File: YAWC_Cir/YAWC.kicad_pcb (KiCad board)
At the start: 2 copper layers, 84 x 35 mm, 32 parts, among them P1 CONN_01X03, P2 TP1a, P3 CONN_5, P4 CONN_5, P5 CONN_6, P6 TP1b, P7 J_AllOff, P8 J_Pot, U1 TPS769XX, U2 SAMD20J18A-M

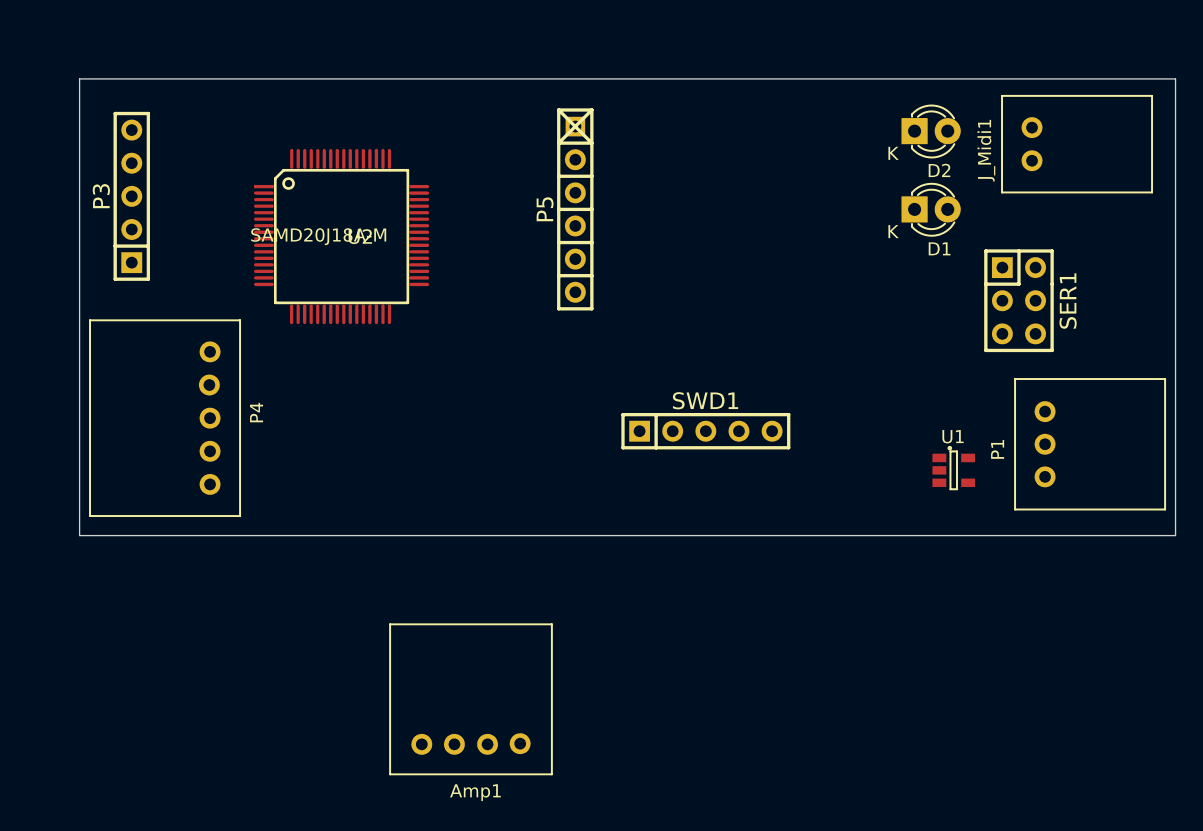
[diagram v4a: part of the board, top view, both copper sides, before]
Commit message: More work on main PCB and positioned connectors to match Keys
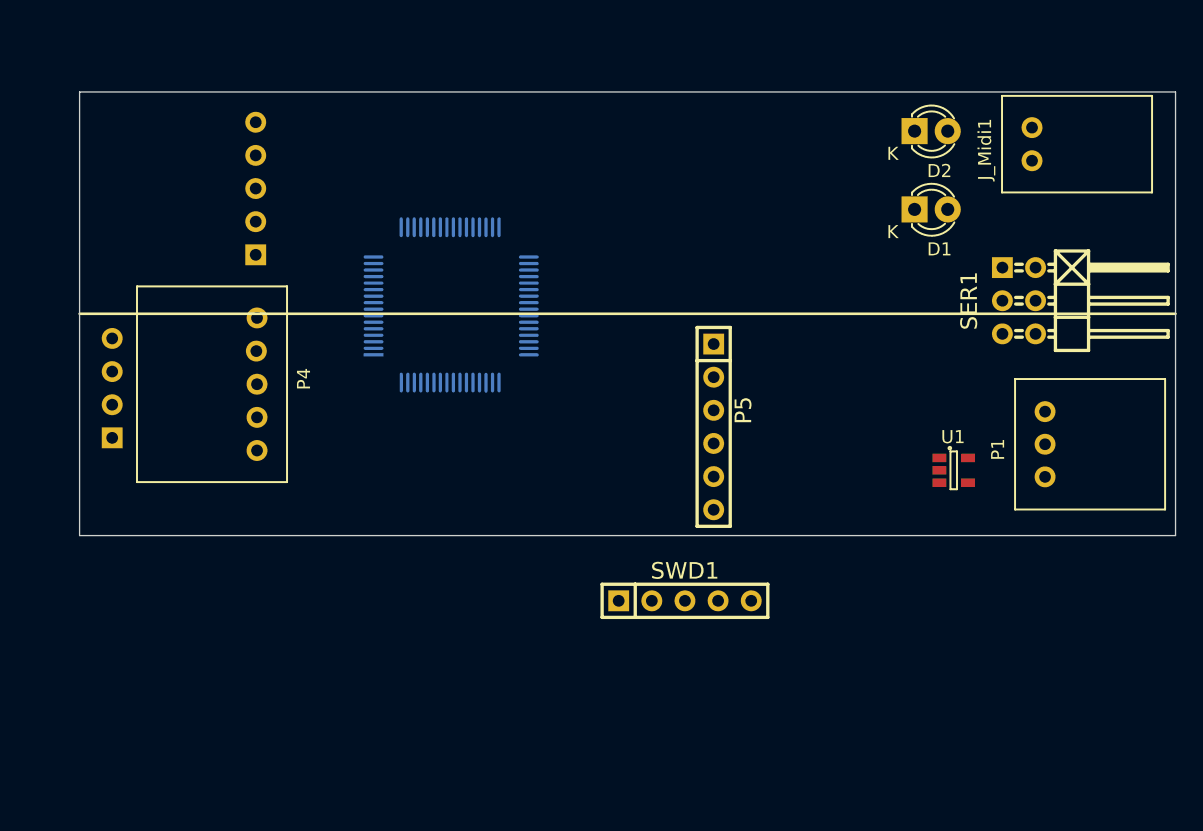
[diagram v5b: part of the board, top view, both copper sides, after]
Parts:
- Amp1: footprint JST:S4B-XH -> PIN_Hdr:Pin_Header_Straight_1x04; moved to B.Cu
- P3, U2: moved to B.Cu
- P5: footprint PIN_Hdr:Pin_Header_1x06 -> PIN_Hdr:Pin_Header_Straight_1x06
- SER1: footprint PIN_Hdr:Pin_Header_Straight_2x03 -> PIN_Hdr:Pin_Header_Angled_2x03
- moved Amp1 38.7 mm to (77.5, 120.7), turned to 90 degrees
- moved P5 18.7 mm to (123.6, 122.4)
- moved SWD1 13.1 mm to (121.4, 137.0)
- moved U2 9.99 mm to (103.4, 114.4), turned to 90 degrees
- moved P3 9.52 mm to (88.5, 105.4)
- moved P4 4.44 mm to (88.6, 120.4)
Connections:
- P3 pad 1: /Micro/Y14 -> /Micro/Y15
- P3 pad 2: /Micro/Y13 -> /Micro/Y2
- P3 pad 3: /Micro/Y12 -> /Micro/Y3
- P3 pad 4: /Micro/Y11 -> /Micro/Y4
- P3 pad 5: /Micro/Y10 -> /Micro/Y5
- P4 pad 1: /Micro/Y15 -> /Micro/Y10
- P4 pad 2: /Micro/Y2 -> /Micro/Y11
- P4 pad 3: /Micro/Y3 -> /Micro/Y12
- P4 pad 4: /Micro/Y4 -> /Micro/Y13
- P4 pad 5: /Micro/Y5 -> /Micro/Y14
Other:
- board size 84 x 35 mm -> 84 x 34 mm

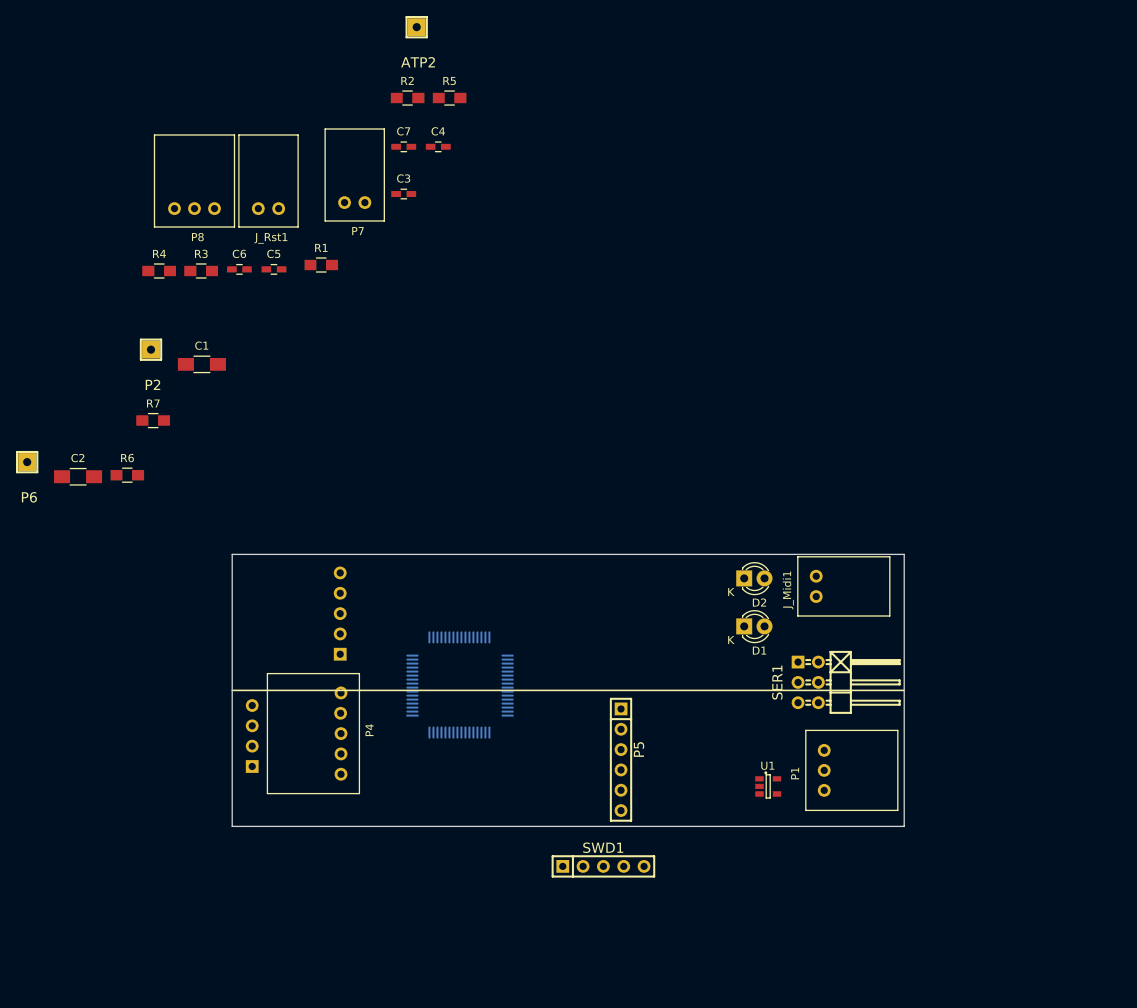
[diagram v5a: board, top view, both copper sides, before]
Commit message: move parts nearer final positions
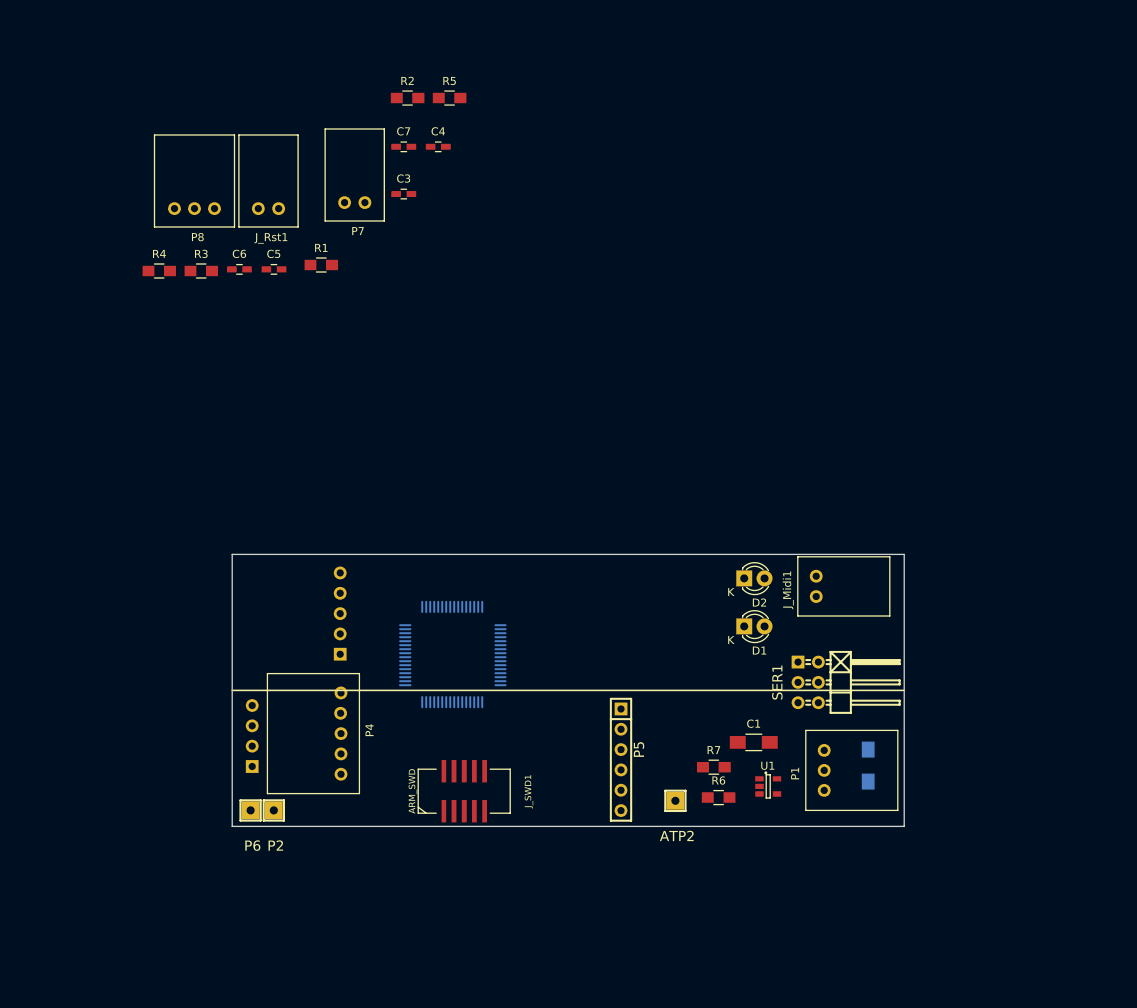
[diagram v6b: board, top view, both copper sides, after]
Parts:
- removed SWD1: CONN_5, PIN_Hdr:Pin_Header_Straight_1x05
- added J_SWD1: ARM_SWD, My_Pin_Headers:2x5_50mil_SMD, F.Cu at (104.0, 127.6)
- C2: moved to B.Cu
- moved C2 105.2 mm to (154.5, 124.4), turned to 90 degrees
- moved ATP2 102.0 mm to (130.4, 128.8)
- moved R6 84.2 mm to (135.8, 128.4)
- moved C1 83.6 mm to (140.2, 121.5)
- moved R7 82.4 mm to (135.2, 124.6)
- moved P2 59.6 mm to (80.2, 130.0)
- moved P6 51.7 mm to (77.3, 130.0)
- moved U2 3.91 mm to (102.5, 110.6)
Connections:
- C1 pad 1: GND -> /VBatt
- P1 pad 3: GND -> /VBatt
- R6 pad 1: GND -> /VBatt
- U1 pad 1: GND -> /VBatt
- U1 pad 4: (no net) -> Net-(U1-Pad4)
- U2 pad 1: (no net) -> Net-(U2-Pad1)
- U2 pad 2: (no net) -> Net-(U2-Pad2)
- U2 pad 23: (no net) -> Net-(U2-Pad23)
- U2 pad 25: (no net) -> Net-(U2-Pad25)
- U2 pad 26: (no net) -> Net-(U2-Pad26)
- U2 pad 27: (no net) -> Net-(U2-Pad27)
- U2 pad 28: (no net) -> Net-(U2-Pad28)
- U2 pad 30: (no net) -> Net-(U2-Pad30)
- U2 pad 31: (no net) -> Net-(U2-Pad31)
- U2 pad 32: (no net) -> Net-(U2-Pad32)
- U2 pad 39: (no net) -> Net-(U2-Pad39)
- U2 pad 40: (no net) -> Net-(U2-Pad40)
- U2 pad 41: (no net) -> Net-(U2-Pad41)
- U2 pad 42: (no net) -> Net-(U2-Pad42)
- U2 pad 43: (no net) -> Net-(U2-Pad43)
- U2 pad 44: (no net) -> Net-(U2-Pad44)
- U2 pad 45: (no net) -> Net-(U2-Pad45)
- U2 pad 46: (no net) -> Net-(U2-Pad46)
- U2 pad 49: (no net) -> Net-(U2-Pad49)
- U2 pad 50: (no net) -> Net-(U2-Pad50)
- U2 pad 51: (no net) -> Net-(U2-Pad51)
- U2 pad 53: (no net) -> Net-(U2-Pad53)

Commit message: Routed but no copper pour
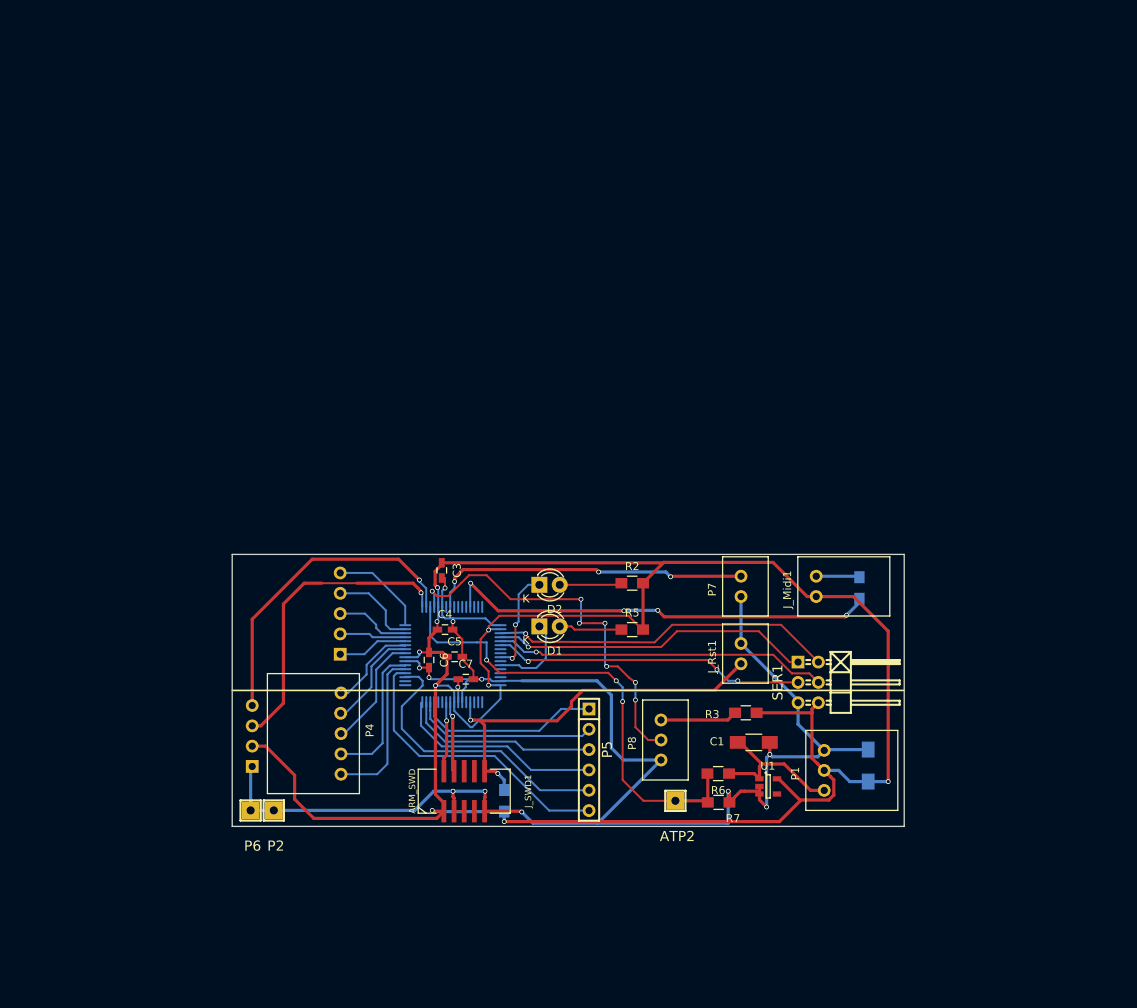
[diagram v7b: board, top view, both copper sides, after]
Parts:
- J_Rst1, P7: footprint JST:S2B-XH -> JST:B2B-XH
- P8: footprint JST:S3B-XH -> JST:B3B-XH
- R1, R4: moved to B.Cu
- moved R4 96.1 mm to (153.4, 102.2), turned to 270 degrees
- moved P8 88.4 mm to (128.6, 121.2), turned to 270 degrees
- moved R3 87.7 mm to (139.2, 117.8), turned to 180 degrees
- moved J_Rst1 81.1 mm to (138.6, 110.4), turned to 270 degrees
- moved R1 70.8 mm to (109.0, 128.8), turned to 90 degrees
- moved R5 70.3 mm to (125.0, 107.4)
- moved P7 68.1 mm to (138.6, 102.0), turned to 270 degrees
- moved C7 67.0 mm to (104.2, 113.6)
- moved R2 66.8 mm to (125.0, 101.6)
- moved C4 60.4 mm to (101.6, 107.4)
- moved C6 54.3 mm to (99.6, 111.2), turned to 270 degrees
- moved C5 53.4 mm to (102.8, 110.8)
- moved C3 47.3 mm to (101.2, 100.0), turned to 270 degrees
- moved D2 25.6 mm to (113.4, 101.8)
- moved D1 25.6 mm to (113.4, 107.0)
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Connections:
- J_SWD1 pad 6: Net-(J_SWD1-Pad6) -> (no net)
- J_SWD1 pad 7: Net-(J_SWD1-Pad7) -> (no net)
- J_SWD1 pad 8: Net-(J_SWD1-Pad8) -> (no net)
- P8 pad 2: Net-(P8-Pad2) -> /Micro/Pot
- R5 pad 1: Net-(D1-Pad1) -> Net-(D1-Pad2)
- SER1 pad 1: /Micro/S1P3 -> /Micro/S1P1
- SER1 pad 2: /Micro/S1P2 -> /Micro/S1P0
- SER1 pad 3: /Micro/S1P1 -> /Micro/S1P3
- SER1 pad 4: /Micro/S1P0 -> /Micro/S1P2
- U1 pad 4: Net-(U1-Pad4) -> (no net)
- U2 pad 1: Net-(U2-Pad1) -> (no net)
- U2 pad 17: Net-(P8-Pad2) -> Bth
- U2 pad 18: BatSample -> Vib
- U2 pad 19: Vib -> BatSample
- U2 pad 2: Net-(U2-Pad2) -> (no net)
- U2 pad 20: Bth -> /Micro/Pot
- U2 pad 23: Net-(U2-Pad23) -> (no net)
- U2 pad 25: Net-(U2-Pad25) -> (no net)
- U2 pad 26: Net-(U2-Pad26) -> (no net)
- U2 pad 27: Net-(U2-Pad27) -> (no net)
- U2 pad 28: Net-(U2-Pad28) -> (no net)
- U2 pad 30: Net-(U2-Pad30) -> (no net)
- U2 pad 31: Net-(U2-Pad31) -> (no net)
- U2 pad 32: Net-(U2-Pad32) -> (no net)
- U2 pad 39: Net-(U2-Pad39) -> (no net)
- U2 pad 40: Net-(U2-Pad40) -> (no net)
- U2 pad 41: Net-(U2-Pad41) -> Net-(D2-Pad1)
- U2 pad 42: Net-(U2-Pad42) -> (no net)
- U2 pad 43: Net-(U2-Pad43) -> Net-(D1-Pad1)
- U2 pad 44: Net-(U2-Pad44) -> (no net)
- U2 pad 45: Net-(U2-Pad45) -> (no net)
- U2 pad 46: Net-(U2-Pad46) -> (no net)
- U2 pad 49: Net-(U2-Pad49) -> (no net)
- U2 pad 50: Net-(U2-Pad50) -> (no net)
- U2 pad 51: Net-(U2-Pad51) -> (no net)
- U2 pad 53: Net-(U2-Pad53) -> (no net)
- U2 pad 59: Net-(D1-Pad2) -> (no net)
- U2 pad 60: Net-(D2-Pad1) -> (no net)
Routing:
- net VCC: track 0.00 -> 289.8 mm, vias 0 -> 9
- net GND: track 0.00 -> 210.2 mm, vias 0 -> 11
- net BatSample: track 0.00 -> 58.6 mm, vias 0 -> 3
- net /Micro/Tx: track 0.00 -> 54.6 mm, vias 0 -> 4
- net /Micro/Reset: track 0.00 -> 50.2 mm, vias 0 -> 2
- net /Micro/Pot: track 0.00 -> 49.0 mm, vias 0 -> 7
- net /Micro/S1P0: track 0.00 -> 43.4 mm, vias 0 -> 1
- net /Micro/S1P2: track 0.00 -> 41.9 mm, vias 0 -> 1
- net Net-(P7-Pad1): track 0.00 -> 40.5 mm, vias 0 -> 3
- net /Micro/S1P1: track 0.00 -> 40.1 mm, vias 0 -> 1
- net Vib: track 0.00 -> 39.6 mm, vias 0 -> 1
- net /Micro/S1P3: track 0.00 -> 39.4 mm, vias 0 -> 3
- net Bth: track 0.00 -> 38.6 mm, vias 0 -> 1
- net /Micro/Y1: track 0.00 -> 36.9 mm
- net /Micro/Y0: track 0.00 -> 36.1 mm
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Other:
- net class Default: trace_width 0.25 -> 0.4
- net class Sense added: clearance 0.2, trace_width 0.25, via_dia 0.6, via_drill 0.4

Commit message: As subbmitted to OSH Park
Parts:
- All Off: renamed from P7
- renumbered ATP2 to ATP, J_Midi1 to Midi, P8 to Pot, P1 to Pwr, J_Rst1 to Rst
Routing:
- net GND: track 210.2 -> 258.7 mm
- added copper zone on B.Cu, net GND
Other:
- board text added: "+"
- board text added: "-"
- board text added: "-+"
- board text added: "0"
- board text added: "1"
- board text added: "2"
- board text added: "3"
- board text added: "Gnd"
- board text added: "YAWC 1.1"
- board text added: "b"
